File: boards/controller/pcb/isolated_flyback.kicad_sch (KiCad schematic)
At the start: 19 parts, among them T2001 150u

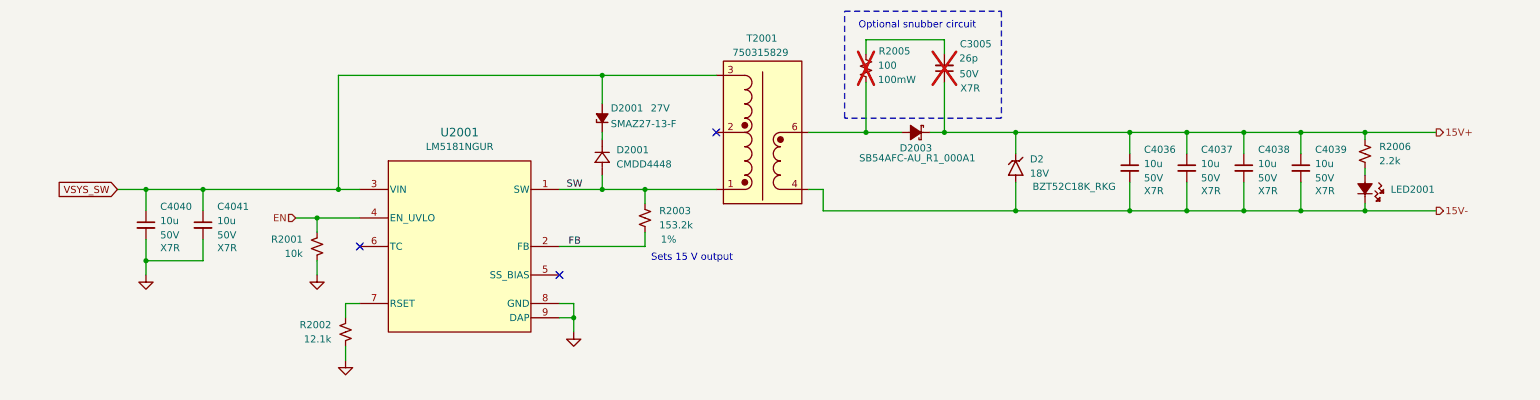
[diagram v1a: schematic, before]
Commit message: controller: pcb: Update schematic
Signed-off-by: Nicholas Loehrke <nicholasnloehrke@gmail.com>
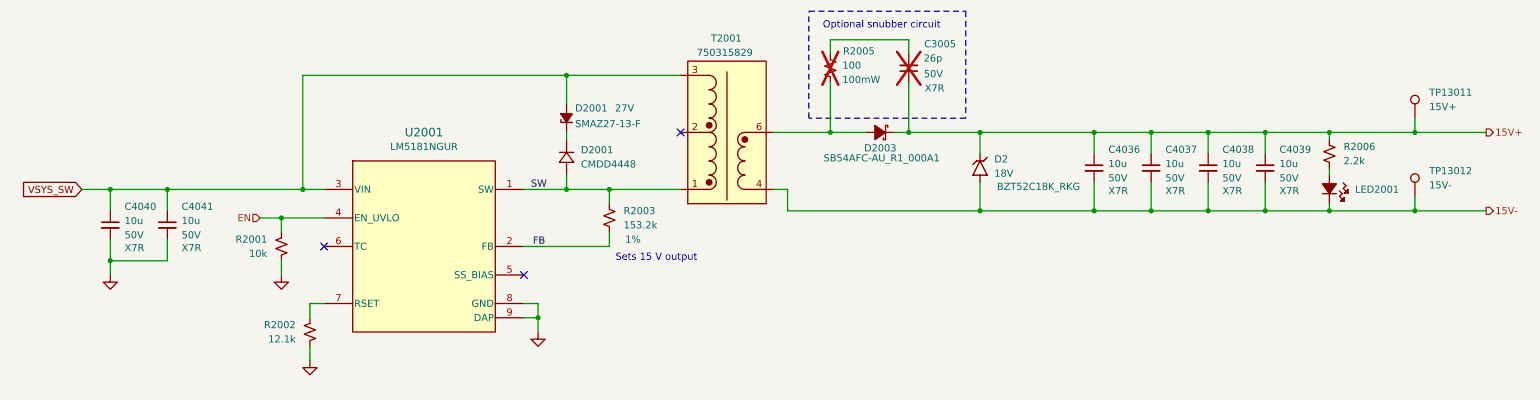
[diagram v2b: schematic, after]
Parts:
- added TP13011: 15V+, symbol Connector:TestPoint
- added TP13012: 15V-, symbol Connector:TestPoint
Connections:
- net 15V+: now also TP13011.1
- net 15V-: now also TP13012.1
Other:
- moved on the sheet: C3005, C4036, C4037, C4038, C4039, C4040, C4041, D2, D2001, D2003, LED2001, R2001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

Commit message: controller: pcb: Update schematic + layout
Signed-off-by: Nicholas Loehrke <nicholasnloehrke@gmail.com>
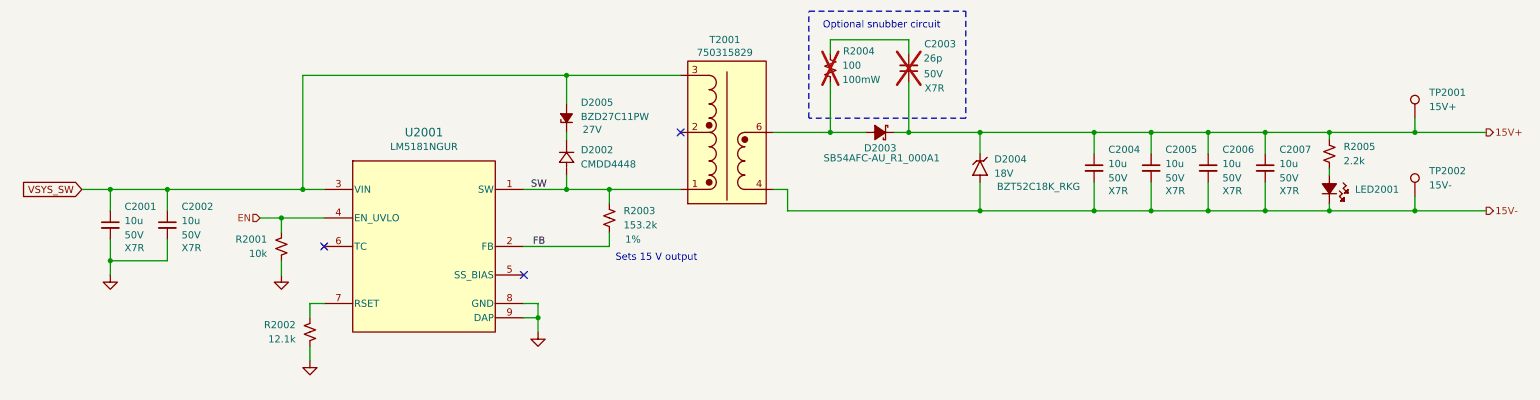
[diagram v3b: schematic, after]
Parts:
- removed D2001: 27V, SMAZ27-13-F:SMAZ27-13-F, symbol SMAZ27-13-F:SMAZ27-13-F
- added D2005: BZD27C11PW, BZD27C11PW:BZD27C11PW, symbol BZD27C11PW:BZD27C11PW
- C2001: renamed from C4040; footprint (none) -> Capacitor_SMD:C_1210_3225Metric
- C2002: renamed from C4041; footprint (none) -> Capacitor_SMD:C_1210_3225Metric
- C2003: renamed from C3005; footprint (none) -> Capacitor_SMD:C_0402_1005Metric
- C2004: renamed from C4036; footprint (none) -> Capacitor_SMD:C_1210_3225Metric
- C2005: renamed from C4037; footprint (none) -> Capacitor_SMD:C_1210_3225Metric
- C2006: renamed from C4038; footprint (none) -> Capacitor_SMD:C_1210_3225Metric
- C2007: renamed from C4039; footprint (none) -> Capacitor_SMD:C_1210_3225Metric
- D2002: renamed from D2001; footprint SOD-323_CNS -> CMDD4448:CMDD4448
- D2003: footprint DIODE_SB54AFC-AU_R1_000A1_PNJ -> SB54AFC-AU_R1_000A1:SB54AFC-AU_R1_000A1
- D2004: renamed from D2; footprint BZT52C18K_RKG:DIO_BZT52C18K_RKG -> BZT52C18K_RKG:BZT52C18K_RKG
- LED2001: footprint LED_B1911PG--20D000514U1930_HVK -> B1911PG--20D000514U1930:B1911PG--20D000514U1930
- R2001, R2002, R2003: footprint Resistor_SMD:R_0603_1608Metric -> Resistor_SMD:R_0402_1005Metric
- R2004: renamed from R2005; footprint Resistor_SMD:R_0603_1608Metric -> Resistor_SMD:R_0805_2012Metric
- R2005: renamed from R2006; footprint (none) -> Resistor_SMD:R_0603_1608Metric
- TP2001: renamed from TP13011; footprint (none) -> TestPoint:TestPoint_Pad_D1.0mm
- TP2002: renamed from TP13012; footprint (none) -> TestPoint:TestPoint_Pad_D1.0mm
- U2001: footprint LM5181NGUR:NGU0008C-IPC_A -> LM5181NGUR:LM5181NGUR-IPC_A
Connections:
- net VSYS_SW: now also D2005.2 (A)
- net at D2002.1: now also D2005.1 (K)

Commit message: controller: Update BOM
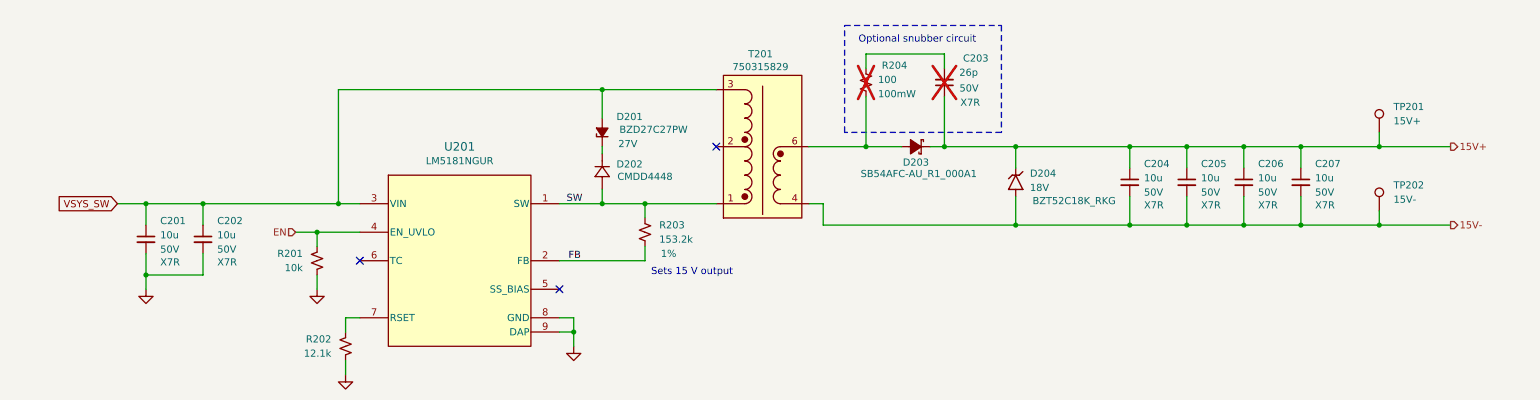
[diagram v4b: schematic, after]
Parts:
- removed LED2001: B1911PG--20D000514U1930, B1911PG--20D000514U1930:B1911PG--20D000514U1930, symbol B1911PG--20D000514U1930:B1911PG--20D000514U1930
- removed R2005: 2.2k, Resistor_SMD:R_0603_1608Metric, symbol Device:R_Small_US
- D201: renamed from D2005; value BZD27C11PW -> BZD27C27PW; MPN (none) -> BZD27C27PW
- D202: renamed from D2002; MPN (none) -> CMDD4448
- D203: renamed from D2003; MPN (none) -> SB54AFC-AU_R1_000A1
- R204: renamed from R2004; footprint Resistor_SMD:R_0805_2012Metric -> Resistor_SMD:R_0402_1005Metric
- renumbered C2001 to C201, C2002 to C202, C2003 to C203, C2004 to C204, C2005 to C205, C2006 to C206, C2007 to C207, D2004 to D204, R2001 to R201, R2002 to R202, R2003 to R203, T2001 to T201, TP2001 to TP201, TP2002 to TP202, U2001 to U201
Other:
- moved on the sheet: C201, C202, C203, C204, C205, C206, C207, D201, D202, D203, D204, R201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
